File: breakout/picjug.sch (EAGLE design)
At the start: 38 parts, among them Q1 BSS138, Q2 BSS138, Q3 BSS84, Q4 BSS84, U1 PIC16F1454SOIC, U2 AP7115W, X1 MINI-USB-UX60-MB-5ST

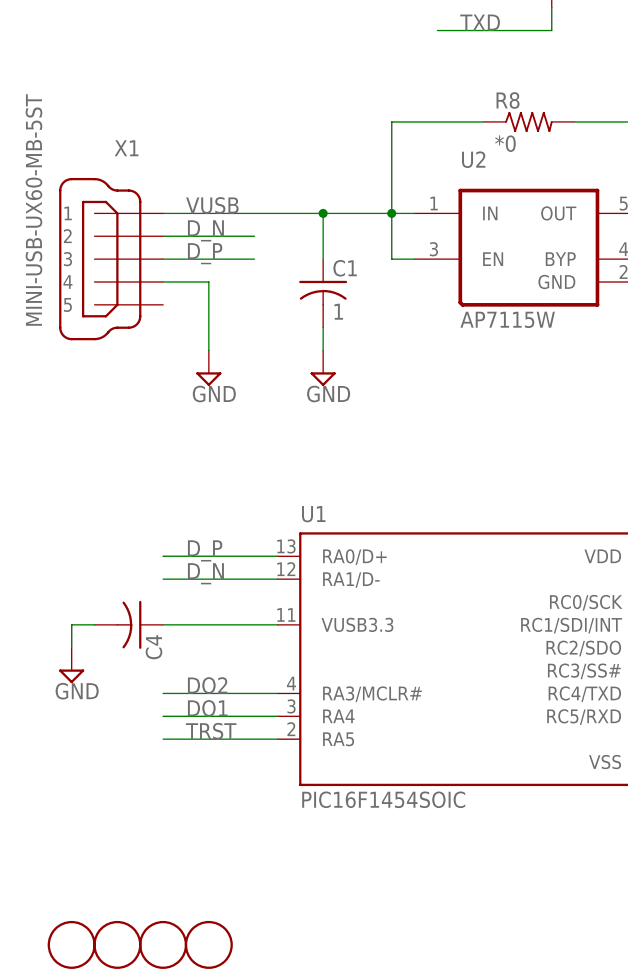
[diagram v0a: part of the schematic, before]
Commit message: add test points for in system programming
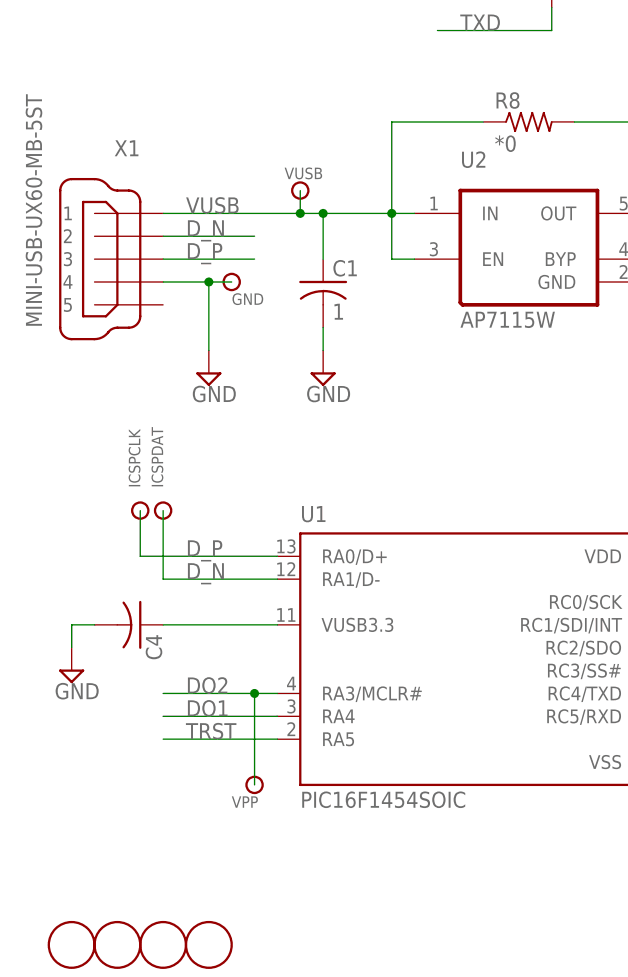
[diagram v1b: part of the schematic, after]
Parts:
- added GND, ICSPCLK, ICSPDAT, VPP, VUSB: TESTPOINTMILLMAX_0900_SMALL, ak-misc:TESTPOINTMILLMAX_0900_SMALL
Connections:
- net DO2: now also VPP.1
- net D_N: now also ICSPDAT.1
- net D_P: now also ICSPCLK.1
- net GND: now also GND.1
- net VUSB: now also VUSB.1
